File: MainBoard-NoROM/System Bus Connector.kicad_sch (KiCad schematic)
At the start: 77 parts, among them J3 71922-164LF

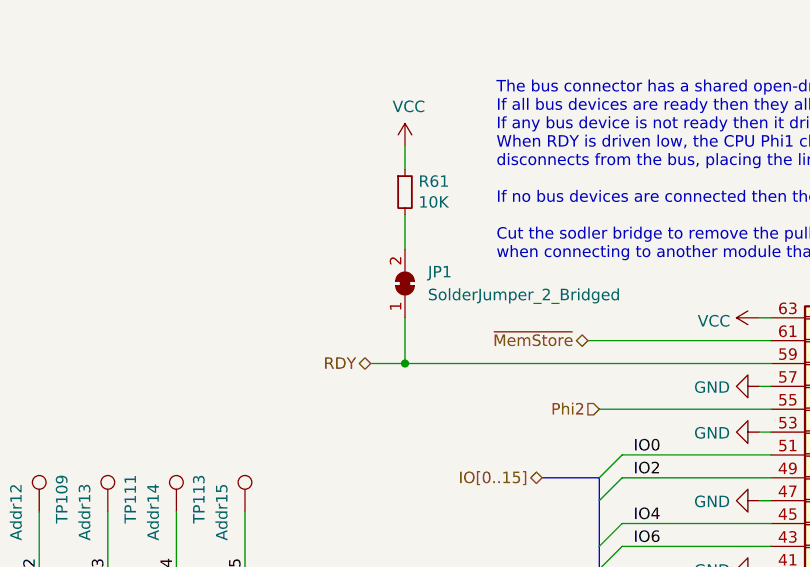
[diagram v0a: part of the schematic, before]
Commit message: MEMModule: Fix bug in the bank register reset signal
The bank register expects an active-high reset signal but was wired to
receive an active-low signal. Fix this issue by routing /RST_sync through
an inverter first.

BUG: The MainBoard PCB layout has not been updated yet.
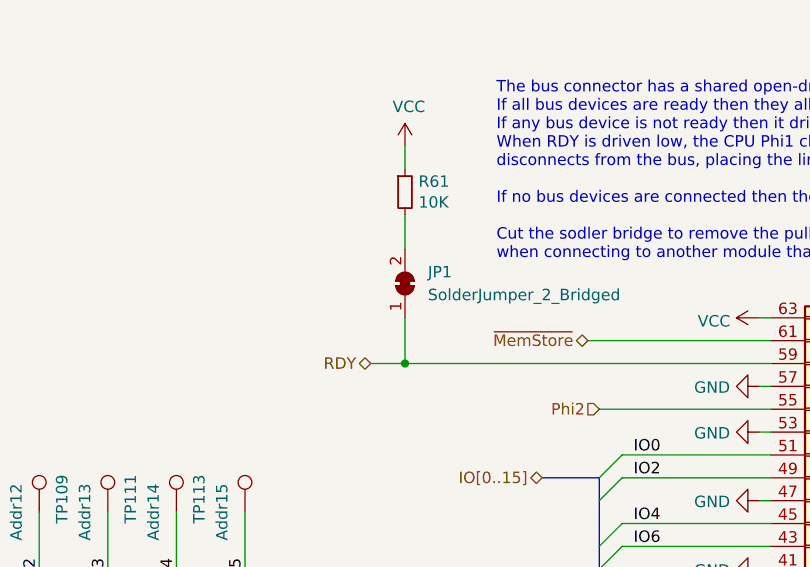
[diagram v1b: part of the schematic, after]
